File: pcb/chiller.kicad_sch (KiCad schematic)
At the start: 57 parts, among them J1 Temp sensor 1, J10 Fan, J11 Display, J12 Debug, J13 Conn_01x04, J14 Flow sensor, J16 Buzzer, J2 Temp sensor 2, J3 Ext, J4 Mains in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

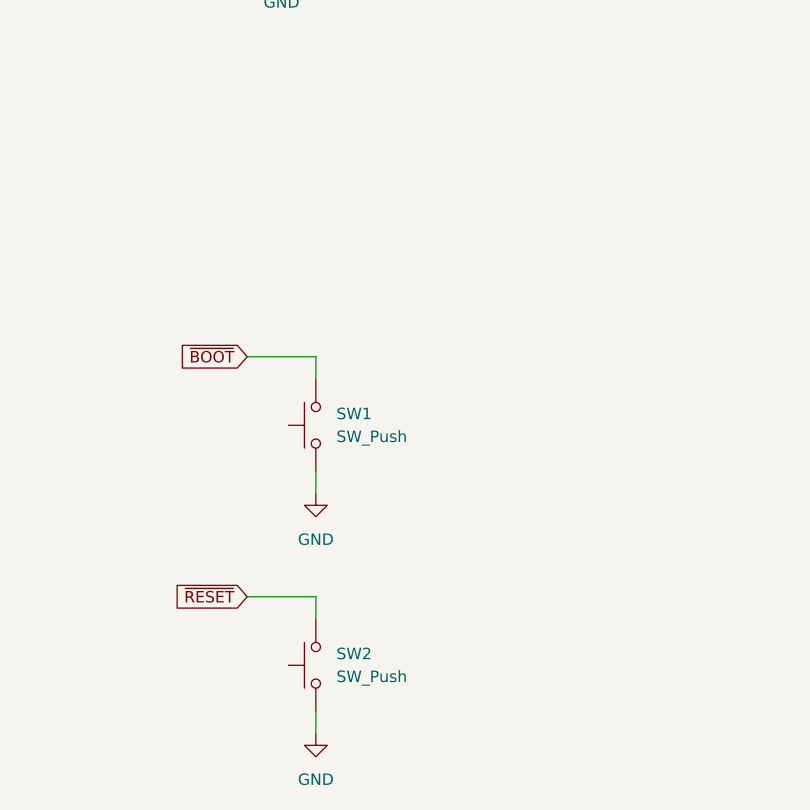
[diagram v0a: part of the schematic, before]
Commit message: Add pullups
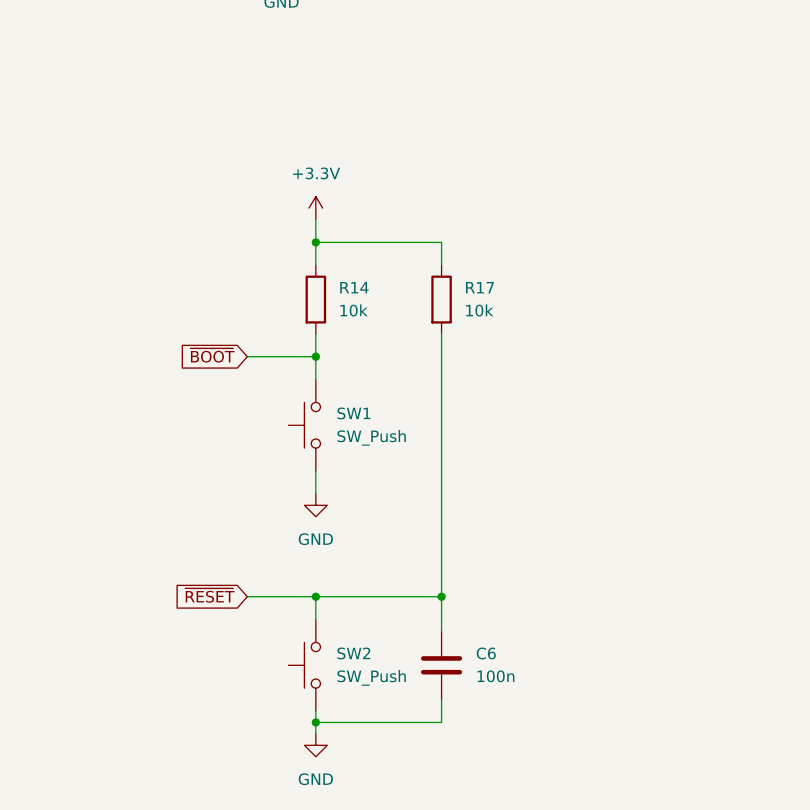
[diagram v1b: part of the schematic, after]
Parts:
- added C6: 100n, symbol Device:C
- added R14, R17: 10k, symbol Device:R
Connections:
- net GND: now also C6.2
- net ~{BOOT}: now also R14.2
- net ~{RESET}: now also C6.1, R17.2
- new net +3.3V: R14.1, R17.1
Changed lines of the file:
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@@
   (junction (at 163.83 130.81) (diameter 0) (color 0 0 0 0)
   )
+  (junction (at 255.27 237.49) (diameter 0) (color 0 0 0 0)
+  )
   (junction (at 57.15 104.14) (diameter 0) (color 0 0 0 0)
   )
@@
   (junction (at 173.99 161.29) (diameter 0) (color 0 0 0 0)
   )
+  (junction (at 241.3 251.46) (diameter 0) (color 0 0 0 0)
+  )
+  (junction (at 241.3 198.12) (diameter 0) (color 0 0 0 0)
+  )
   (junction (at 176.53 203.2) (diameter 1.016) (color 0 0 0 0)
   )
@@
   (junction (at 123.19 162.56) (diameter 0) (color 0 0 0 0)
   )
+  (junction (at 241.3 210.82) (diameter 0) (color 0 0 0 0)
+  )
   (junction (at 121.92 175.26) (diameter 0) (color 0 0 0 0)
   )
@@
   (junction (at 252.73 49.53) (diameter 0) (color 0 0 0 0)
   )
+  (junction (at 241.3 237.49) (diameter 0) (color 0 0 0 0)
+  )
   (junction (at 163.83 149.86) (diameter 0) (color 0 0 0 0)
   )
@@
     (stroke (width 0) (type default))
   )
+  (wire (pts (xy 241.3 251.46) (xy 241.3 252.73))
+    (stroke (width 0) (type default))
+  )
   (wire (pts (xy 57.15 101.6) (xy 57.15 104.14))
     (stroke (width 0) (type default))
@@
     (stroke (width 0) (type default))
   )
+  (wire (pts (xy 255.27 237.49) (xy 255.27 241.3))
+    (stroke (width 0) (type default))
+  )
   (wire (pts (xy 33.02 43.18) (xy 33.02 45.72))
     (stroke (width 0) (type default))
@@
     (stroke (width 0) (type default))
   )
+  (wire (pts (xy 255.27 248.92) (xy 255.27 251.46))
+    (stroke (width 0) (type default))
+  )
   (wire (pts (xy 57.15 104.14) (xy 57.15 106.68))
     (stroke (width 0) (type default))
@@
     (stroke (width 0) (type default))
   )
+  (wire (pts (xy 255.27 237.49) (xy 241.3 237.49))
+    (stroke (width 0) (type default))
+  )
   (wire (pts (xy 88.9 59.69) (xy 93.98 59.69))
     (stroke (width 0) (type default))
@@
     (stroke (width 0) (type default))
   )
+  (wire (pts (xy 255.27 208.28) (xy 255.27 237.49))
+    (stroke (width 0) (type default))
+  )
   (wire (pts (xy 170.18 82.55) (xy 170.18 88.9))
     (stroke (width 0) (type default))
@@
     (stroke (width 0) (type default))
   )
+  (wire (pts (xy 255.27 198.12) (xy 241.3 198.12))
+    (stroke (width 0) (type default))
+  )
   (wire (pts (xy 124.46 68.58) (xy 134.62 68.58))
     (stroke (width 0) (type default))
@@
     (stroke (width 0) (type default))
   )
+  (wire (pts (xy 255.27 251.46) (xy 241.3 251.46))
+    (stroke (width 0) (type default))
+  )
   (wire (pts (xy 171.45 161.29) (xy 173.99 161.29))
     (stroke (width 0) (type default))
@@
     (stroke (width 0) (type default))
   )
+  (wire (pts (xy 255.27 200.66) (xy 255.27 198.12))
+    (stroke (width 0) (type default))
+  )
   (wire (pts (xy 156.21 233.68) (xy 156.21 240.03))
     (stroke (width 0) (type solid))
@@
     (stroke (width 0) (type default))
   )
+  (wire (pts (xy 241.3 208.28) (xy 241.3 210.82))
+    (stroke (width 0) (type default))
+  )
   (wire (pts (xy 50.8 119.38) (xy 57.15 119.38))
     (stroke (width 0) (type default))
@@
     (stroke (width 0) (type default))
   )
+  (wire (pts (xy 241.3 195.58) (xy 241.3 198.12))
+    (stroke (width 0) (type default))
+  )
   (wire (pts (xy 121.92 165.1) (xy 121.92 175.26))
     (stroke (width 0) (type default))
@@
     (stroke (width 0) (type default))
   )
+  (wire (pts (xy 241.3 198.12) (xy 241.3 200.66))
+    (stroke (width 0) (type default))
+  )
   (wire (pts (xy 24.13 83.82) (xy 24.13 78.74))
     (stroke (width 0) (type default))
@@
     (stroke (width 0) (type default))
   )
-  (wire (pts (xy 241.3 250.19) (xy 241.3 252.73))
+  (wire (pts (xy 241.3 250.19) (xy 241.3 251.46))
     (stroke (width 0) (type default))
   )
@@
     (effects (font (size 1.27 1.27)) (justify left))
   )
+  (symbol (lib_id "Device:C") (at 255.27 245.11 0) (unit 1)
+    (exclude_from_sim no) (in_bom yes) (on_board yes) (dnp no) (fields_autoplaced)
+    (property "Reference" "C6" (at 259.08 243.8399 0)
+      (effects (font (size 1.27 1.27)) (justify left))
+    )
+    (property "Value" "100n" (at 259.08 246.3799 0)
+      (effects (font (size 1.27 1.27)) (justify left))
+    )
+    (property "Footprint" "" (at 256.2352 248.92 0)
+      (effects (font (size 1.27 1.27)) hide)
+    )
+    (property "Datasheet" "~" (at 255.27 245.11 0)
+      (effects (font (size 1.27 1.27)) hide)
+    )
+    (property "Description" "Unpolarized capacitor" (at 255.27 245.11 0)
+      (effects (font (size 1.27 1.27)) hide)
+    )
+    (pin "1")
+    (pin "2")
+    (instances
+      (project "chiller"
+        (path "/212a0d71-cc7b-49f8-b4ca-a935e5355dca"
+          (reference "C6") (unit 1)
+        )
+      )
+    )
+  )
   (symbol (lib_id "power:+3V3") (at 127 50.8 0) (unit 1)
     (exclude_from_sim no) (in_bom yes) (on_board yes) (dnp no)
@@
     )
   )
+  (symbol (lib_id "Device:R") (at 255.27 204.47 0) (unit 1)
+    (exclude_from_sim no) (in_bom yes) (on_board yes) (dnp no) (fields_autoplaced)
+    (property "Reference" "R17" (at 257.81 203.1999 0)
+      (effects (font (size 1.27 1.27)) (justify left))
+    )
+    (property "Value" "10k" (at 257.81 205.7399 0)
+      (effects (font (size 1.27 1.27)) (justify left))
+    )
+    (property "Footprint" "" (at 253.492 204.47 90)
+      (effects (font (size 1.27 1.27)) hide)
+    )
+    (property "Datasheet" "~" (at 255.27 204.47 0)
+      (effects (font (size 1.27 1.27)) hide)
+    )
+    (property "Description" "Resistor" (at 255.27 204.47 0)
+      (effects (font (size 1.27 1.27)) hide)
+    )
+    (pin "1")
+    (pin "2")
+    (instances
+      (project "chiller"
+        (path "/212a0d71-cc7b-49f8-b4ca-a935e5355dca"
+          (reference "R17") (unit 1)
+        )
+      )
+    )
+  )
   (symbol (lib_id "power:+3V3") (at 57.15 101.6 0) (unit 1)
     (exclude_from_sim no) (in_bom yes) (on_board yes) (dnp no) (fields_autoplaced)
@@
     )
   )
+  (symbol (lib_id "power:+3.3V") (at 241.3 195.58 0) (unit 1)
+    (exclude_from_sim no) (in_bom yes) (on_board yes) (dnp no) (fields_autoplaced)
+    (property "Reference" "#PWR09" (at 241.3 199.39 0)
+      (effects (font (size 1.27 1.27)) hide)
+    )
+    (property "Value" "+3.3V" (at 241.3 190.5 0)
+      (effects (font (size 1.27 1.27)))
+    )
+    (property "Footprint" "" (at 241.3 195.58 0)
+      (effects (font (size 1.27 1.27)) hide)
+    )
+    (property "Datasheet" "" (at 241.3 195.58 0)
+      (effects (font (size 1.27 1.27)) hide)
+    )
+    (property "Description" "Power flag, +3.3V" (at 241.3 195.58 0)
+      (effects (font (size 1.27 1.27)) hide)
+    )
+    (pin "1")
+    (instances
+      (project "chiller"
+        (path "/212a0d71-cc7b-49f8-b4ca-a935e5355dca"
+          (reference "#PWR09") (unit 1)
+        )
+      )
+    )
+  )
   (symbol (lib_id "power:GND") (at 215.9 134.62 0) (unit 1)
     (exclude_from_sim no) (in_bom yes) (on_board yes) (dnp no) (fields_autoplaced)
@@
         )
       )
+    )
+  )
+  (symbol (lib_id "Device:R") (at 241.3 204.47 0) (unit 1)
+    (exclude_from_sim no) (in_bom yes) (on_board yes) (dnp no) (fields_autoplaced)
+    (property "Reference" "R14" (at 243.84 203.1999 0)
+      (effects (font (size 1.27 1.27)) (justify left))
+    )
+    (property "Value" "10k" (at 243.84 205.7399 0)
+      (effects (font (size 1.27 1.27)) (justify left))
+    )
+    (property "Footprint" "" (at 239.522 204.47 90)
+      (effects (font (size 1.27 1.27)) hide)
+    )
+    (property "Datasheet" "~" (at 241.3 204.47 0)
+      (effects (font (size 1.27 1.27)) hide)
+    )
+    (property "Description" "Resistor" (at 241.3 204.47 0)
+      (effects (font (size 1.27 1.27)) hide)
+    )
+    (pin "1")
+    (pin "2")
+    (instances
+      (project "chiller"
+        (path "/212a0d71-cc7b-49f8-b4ca-a935e5355dca"
+          (reference "R14") (unit 1)
+        )
+      )

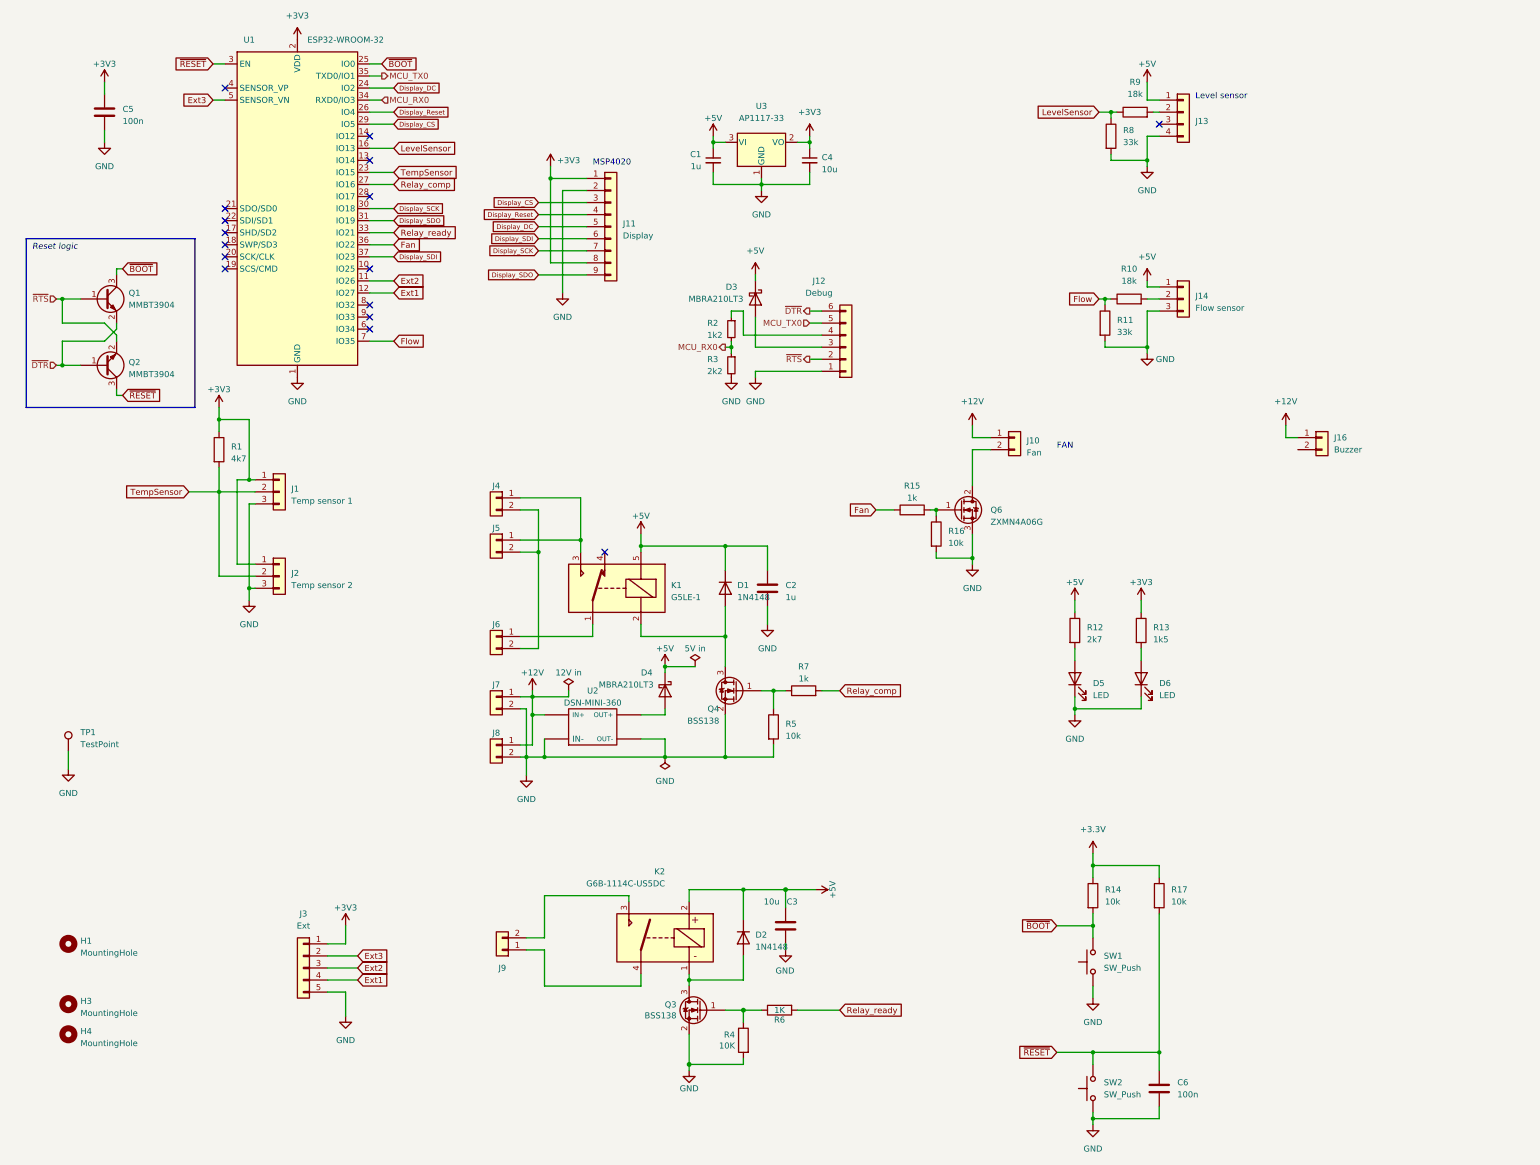
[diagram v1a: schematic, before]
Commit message: Add missing components.
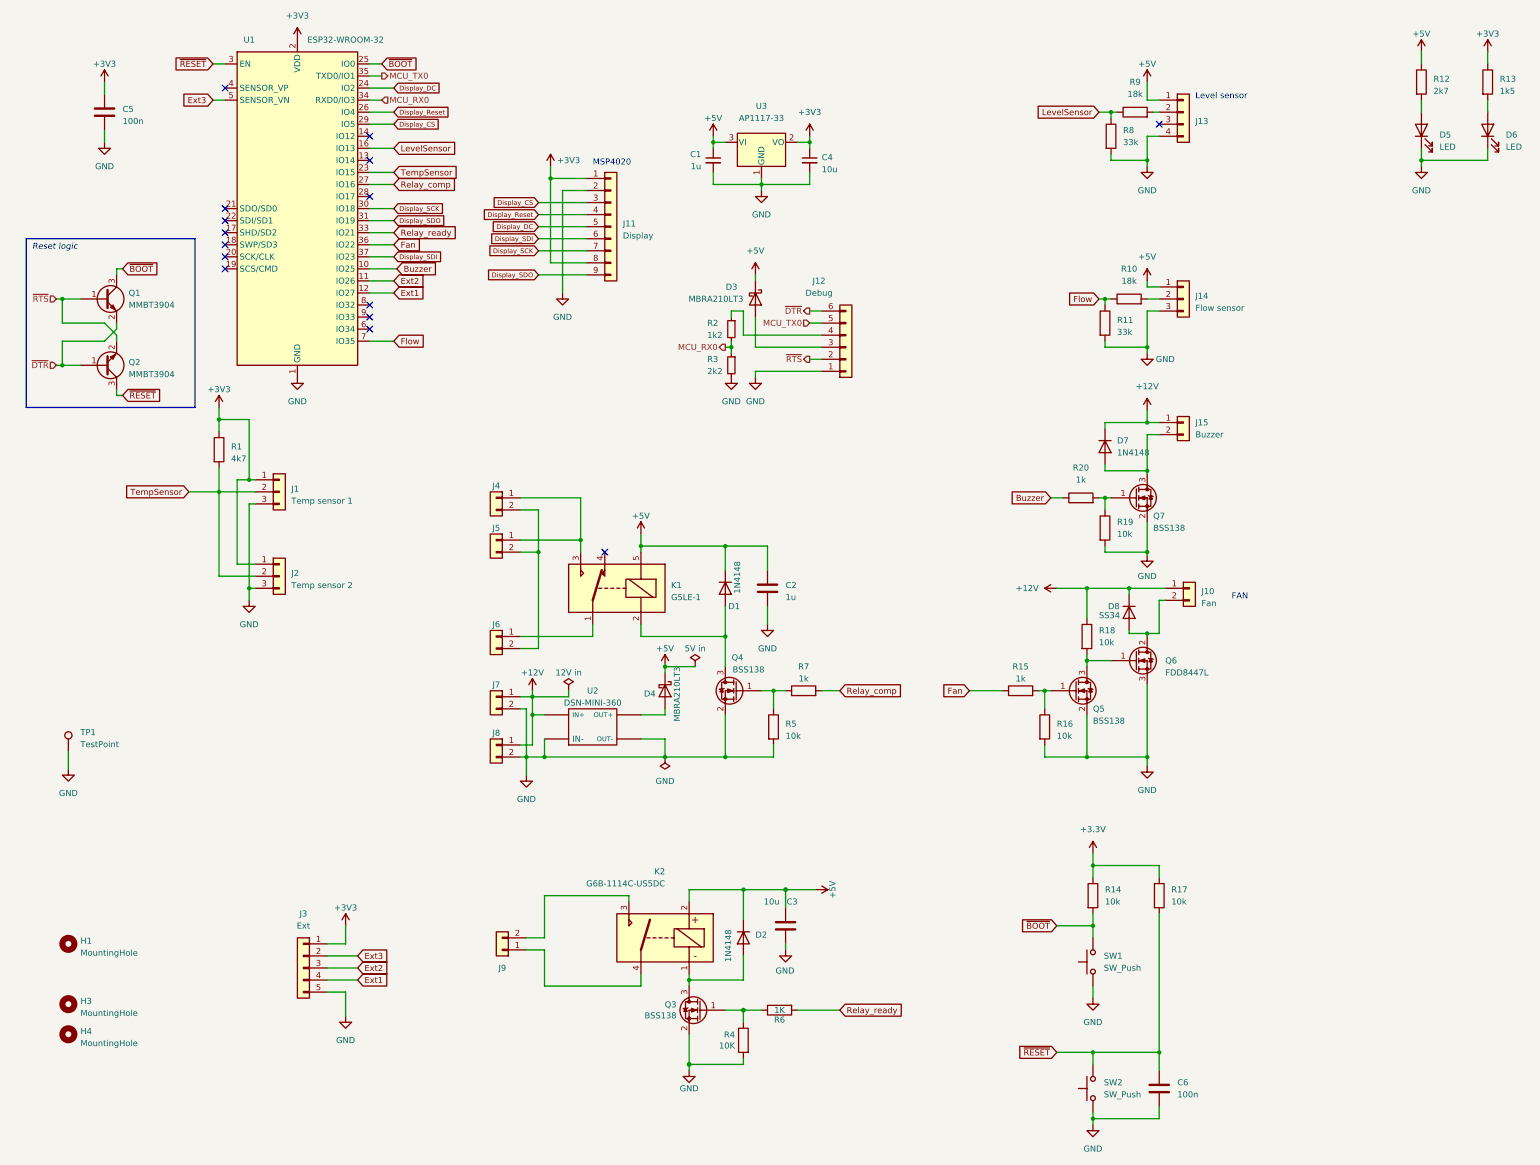
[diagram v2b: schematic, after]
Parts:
- added D7: 1N4148, Diode_SMD:D_SOD-123, symbol Device:D
- added D8: SS34, Diode_SMD:D_SMC, symbol Device:D
- added Q5, Q7: BSS138, Package_TO_SOT_SMD:SOT-23, symbol Device:Q_NMOS_GSD
- added R18, R19: 10k, Resistor_SMD:R_0603_1608Metric, symbol Device:R
- added R20: 1k, Resistor_SMD:R_0603_1608Metric, symbol Device:R
- C6: footprint (none) -> Capacitor_SMD:C_0603_1608Metric
- Q6: value ZXMN4A06G -> FDD8447L; footprint Package_TO_SOT_SMD:SOT-223-3_TabPin2 -> Package_TO_SOT_SMD:TO-252-2
- R14, R17: footprint (none) -> Resistor_SMD:R_0603_1608Metric
- renumbered J16 to J15
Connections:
- net +12V: now also D7.1 (K), D8.1 (K), R18.1
- net GND: now also Q5.2 (S), Q7.2 (S), R19.2
- net at J10.2 (Pin_2), Q6.2 (D): now also D8.2 (A)
- net Buzzer: now reaches U1.10 (IO25)
- net Buzzer: now also R20.1
- net at R15.2, R16.1: now also Q5.1 (G); no longer Q6.1 (G)
- net at J15.2 (Pin_2): now also D7.2 (A), Q7.3 (D)
- new net: Q7.1 (G), R19.1, R20.2
- new net: Q5.3 (D), Q6.1 (G), R18.2
- no-connect marks 16 -> 15
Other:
- moved on the sheet: D5, D6, J10, J15, Q6, R12, R13, R15, R16

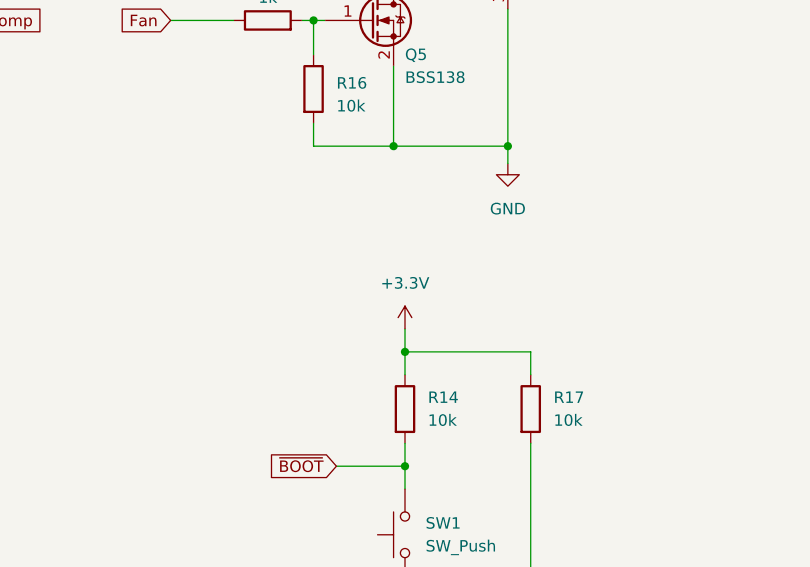
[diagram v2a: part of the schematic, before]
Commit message: Place all components.
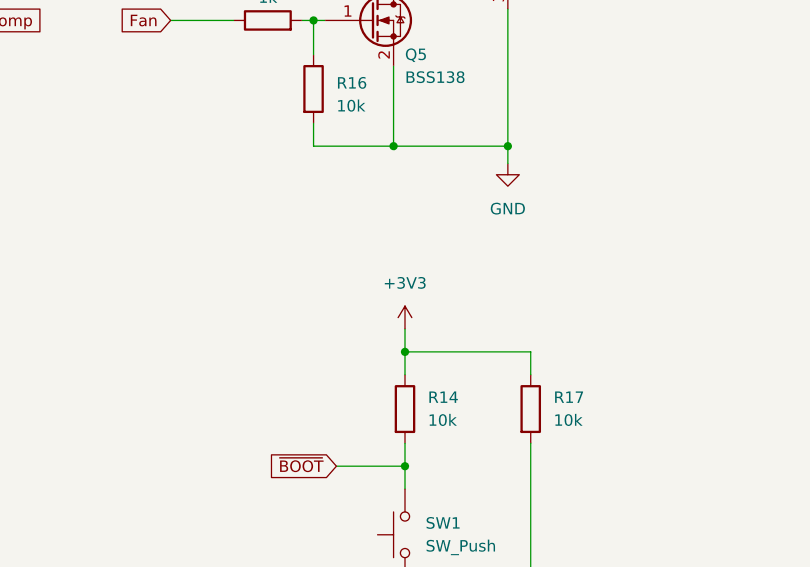
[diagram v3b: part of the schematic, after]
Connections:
- net +3.3V is gone; now on net +3V3: R14.1, R17.1
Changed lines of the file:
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@@
+    )
+  )
+  (symbol (lib_id "power:+3V3") (at 241.3 195.58 0) (unit 1)
+    (exclude_from_sim no) (in_bom yes) (on_board yes) (dnp no) (fields_autoplaced)
+    (property "Reference" "#PWR09" (at 241.3 199.39 0)
+      (effects (font (size 1.27 1.27)) hide)
+    )
+    (property "Value" "+3V3" (at 241.3 190.5 0)
+      (effects (font (size 1.27 1.27)))
+    )
+    (property "Footprint" "" (at 241.3 195.58 0)
+      (effects (font (size 1.27 1.27)) hide)
+    )
+    (property "Datasheet" "" (at 241.3 195.58 0)
+      (effects (font (size 1.27 1.27)) hide)
+    )
+    (property "Description" "Power flag, +3.3V" (at 241.3 195.58 0)
+      (effects (font (size 1.27 1.27)) hide)
+    )
+    (pin "1")
+    (instances
+      (project "chiller"
+        (path "/212a0d71-cc7b-49f8-b4ca-a935e5355dca"
+          (reference "#PWR09") (unit 1)
+        )
+      )
     )
   )
@@
         )
       )
-    )
-  )
-  (symbol (lib_id "power:+3.3V") (at 241.3 195.58 0) (unit 1)
-    (exclude_from_sim no) (in_bom yes) (on_board yes) (dnp no) (fields_autoplaced)
-    (property "Reference" "#PWR09" (at 241.3 199.39 0)
-      (effects (font (size 1.27 1.27)) hide)
-    )
-    (property "Value" "+3.3V" (at 241.3 190.5 0)
-      (effects (font (size 1.27 1.27)))
-    )
-    (property "Footprint" "" (at 241.3 195.58 0)
-      (effects (font (size 1.27 1.27)) hide)
-    )
-    (property "Datasheet" "" (at 241.3 195.58 0)
-      (effects (font (size 1.27 1.27)) hide)
-    )
-    (property "Description" "Power flag, +3.3V" (at 241.3 195.58 0)
-      (effects (font (size 1.27 1.27)) hide)
-    )
-    (pin "1")
-    (instances
-      (project "chiller"
-        (path "/212a0d71-cc7b-49f8-b4ca-a935e5355dca"
-          (reference "#PWR09") (unit 1)
-        )
-      )
